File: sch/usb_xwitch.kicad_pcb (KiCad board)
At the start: 4 copper layers, 84 x 56.5 mm, 136 parts, among them J1 USB_B_Micro, J10 USB_A, J12 Screw_Terminal_3.5mm, J13 Conn_02x05_Odd_Even, J14 Screw_Terminal_3.5mm, J15 Screw_Terminal_3.5mm, J3 USB3_A, J4 USB_C_Receptacle, J5 USB3_A, J6 USB_A, J7 USB_A, J8 USB_B, J9 USB_A, K1 Relay_DPDT_Panasonic_AGQ200A4H, Q1 2N7002P, Q2 2N7002P, SW1 C2689642, SW2 C2689642, U2 W25Q64JVSSIQ, U3 RP2040, U4 FSUSB42MUX, U5 MIC2026-1BM, U6 MIC2026-1BM, U7 USB2514B_Bi, U8 MP1584EN-LF-Z, U9 NCP1117LPST33T3G, Y1 12MHz, Y2 24MHz

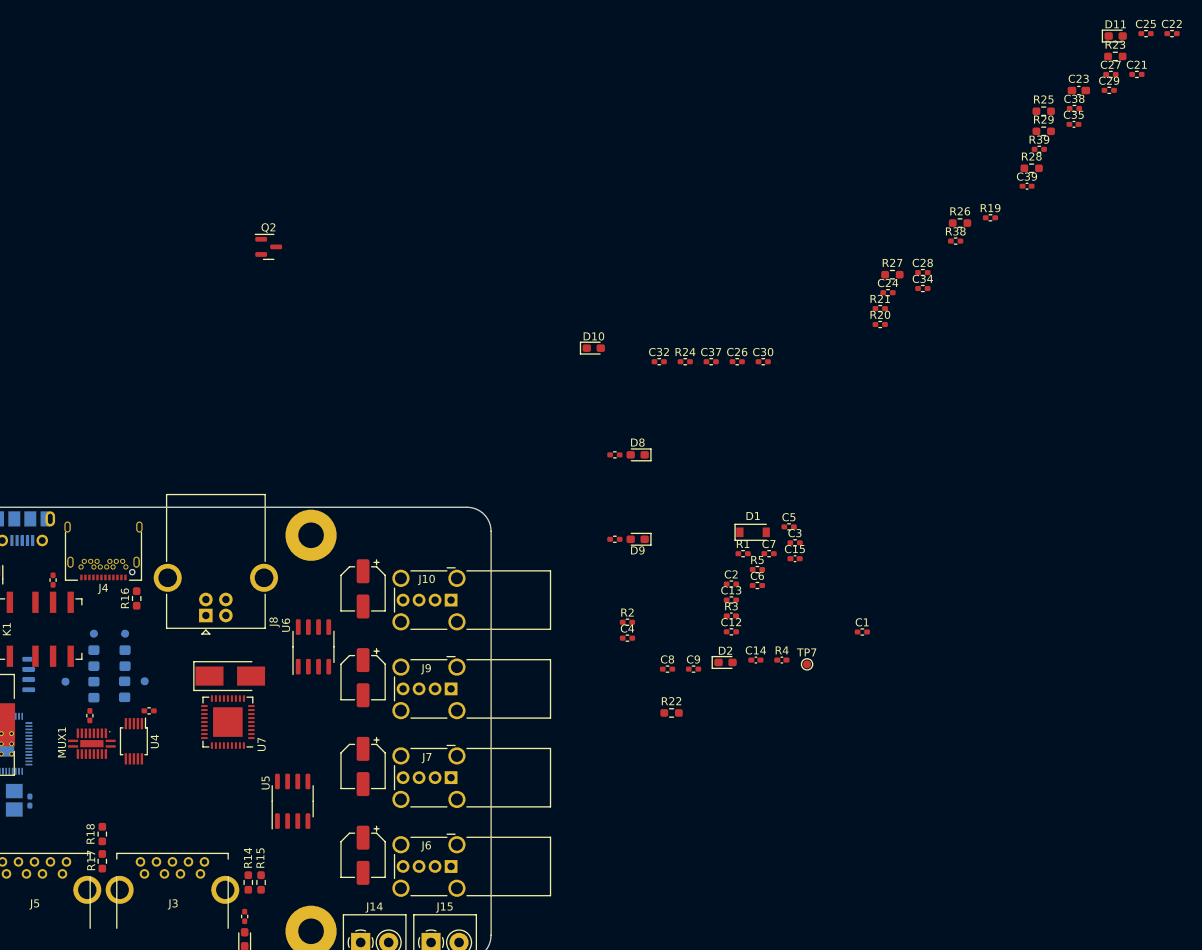
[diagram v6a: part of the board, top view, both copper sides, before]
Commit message: update component layout
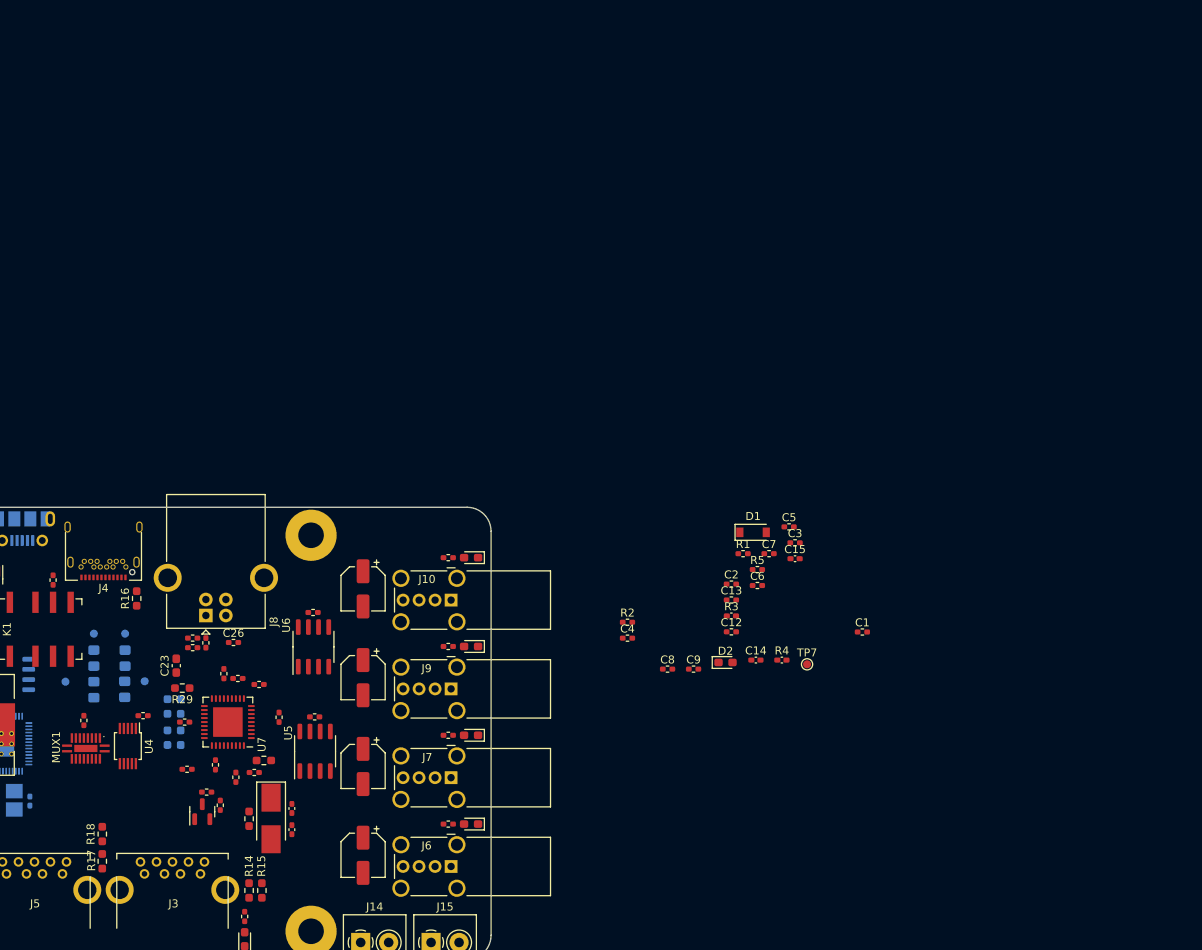
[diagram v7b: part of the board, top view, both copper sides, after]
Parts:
- R25, R26, R27, R28: moved to B.Cu
- moved C25 147.8 mm to (145.7, 106.8), turned to 180 degrees
- moved R23 144.2 mm to (153.8, 118.9), turned to 90 degrees
- moved C29 140.0 mm to (149.6, 112.2), turned to -90 degrees
- moved C23 133.8 mm to (144.7, 99.8), turned to 90 degrees
- moved C27 131.4 mm to (157.5, 106.2), turned to 90 degrees
- moved R25 131.1 mm to (145.2, 104.9), turned to -90 degrees
- moved C21 130.4 mm to (161.9, 106.2)
- moved C35 129.9 mm to (159.1, 117.7), turned to -90 degrees
- moved C22 129.5 mm to (161.8, 93.2)
- moved R28 129.4 mm to (143.6, 108.8), turned to -90 degrees
- moved R29 128.2 mm to (145.4, 102.6), turned to 180 degrees
- moved C38 126.5 mm to (152.3, 101.4)
- moved C39 122.1 mm to (159.1, 120.3), turned to -90 degrees
- moved R26 116.7 mm to (145.2, 108.8), turned to 90 degrees
- moved R19 111.5 mm to (148.3, 97.0), turned to -90 degrees
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
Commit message: update components layout
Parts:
- C1, C12, C13, C14, C15, C2, C3, C4, C5, C6, C7, C8, C9, D1, R1, R2, R3, R4, TP7: moved to B.Cu
- J1: moved to F.Cu
- moved TP7 153.9 mm to (70.6, 82.5), turned to 180 degrees
- moved C15 150.9 mm to (72.1, 69.3), turned to 180 degrees
- moved C3 150.9 mm to (72.1, 67.3), turned to 180 degrees
- moved C5 149.4 mm to (72.9, 65.3), turned to 180 degrees
- moved C7 144.4 mm to (75.4, 68.7), turned to 180 degrees
- moved C6 141.5 mm to (76.8, 72.6), turned to 180 degrees
- moved C14 141.1 mm to (77.0, 82.0), turned to 180 degrees
- moved D1 140.4 mm to (77.4, 66.0), turned to 180 degrees
- moved R1 138.0 mm to (78.6, 68.7), turned to 180 degrees
- moved R3 135.1 mm to (80.1, 76.4), turned to 180 degrees
- moved C9 125.7 mm to (84.8, 83.1), turned to 180 degrees
- moved C1 120.9 mm to (109.5, 94.3), turned to 180 degrees
- moved C8 119.3 mm to (88.0, 83.1), turned to 180 degrees
- moved R5 112.7 mm to (105.4, 101.0)
- moved D2 110.8 mm to (102.5, 101.0)
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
